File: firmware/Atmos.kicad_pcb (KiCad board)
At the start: 4 copper layers, 74 x 56 mm, 73 parts, among them J1 AS3935 breakout, J2 BME280 breakout, J3 USB_C_Receptacle_USB2.0_16P, J4 Micro_SD_Card, J5 Solar power input, J6 Amphenol 132134, Q1 PMOS_Substrate, Q2 PMOS_Substrate, Q3 PMOS_Substrate, SW2 SW_Push, U1 ESP32-S3-WROOM-1, U10 TPS22918DBVR, U11 MAX17048G_T10, U12 CN3791, U13 SGP40-D-R4, U2 AP2112K-3.3, U3 DS3231M, U4 PMS5003, U5 LTC4412xS6, U7 RFM95W-915S2, U8 USBLC6-2SC6, U9 TPS61023DRLR

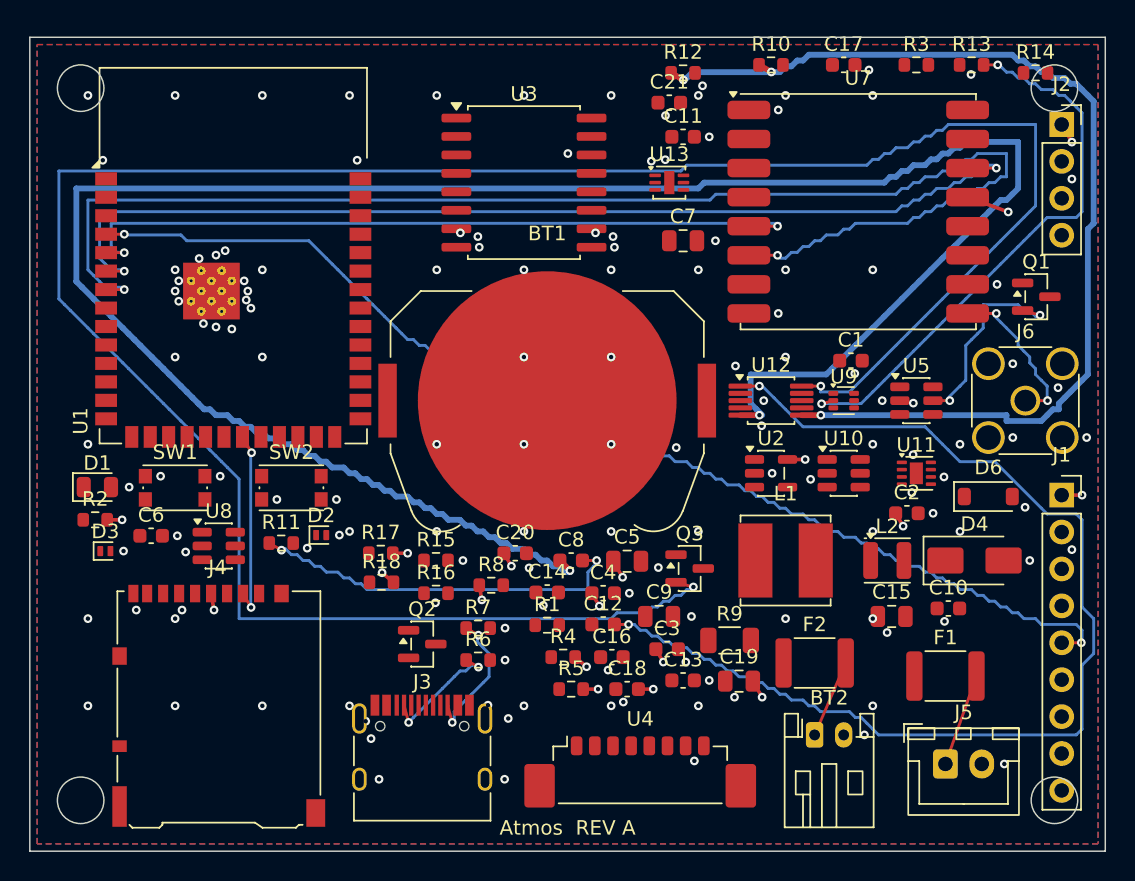
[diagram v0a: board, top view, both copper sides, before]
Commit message: PCB V1: finish routing with Freerouting (~99.85%, solid GND plane)
Completed the remaining ~45% of the board with Freerouting 2.2.4 (headless
CLI, local JRE). From 55% -> ~99.85% routed (1 of ~660 connections open),
0 shorts / 0 clearance / 0 hole-to-hole violations.

- Stackup: F.Cu signal / In1 solid GND plane / In2 +3V3+power+signal / B.Cu
  signal. Freeing In2 as a routing layer (vs locking both inner planes) was
  the key to a completable route.
- F.Cu GND pour stitched to the In1 plane with all-layer/hole/edge-aware vias.
- min_via_diameter 0.5 -> 0.4 mm (Freerouting emits 0.48 mm vias).
- 1 open connection: U13 (SGP40) GND, blocked by the placeholder DFN
  footprint; resolves when the real 2.44 mm land is placed.
- Respin note: move R14 (edge placement) next to U9.

Adds the reproducible Freerouting pipeline under tools/ and a full write-up
in docs/PCB-V1-NOTES.md.

Co-Authored-By: Claude Opus 4.8 <noreply@anthropic.com>
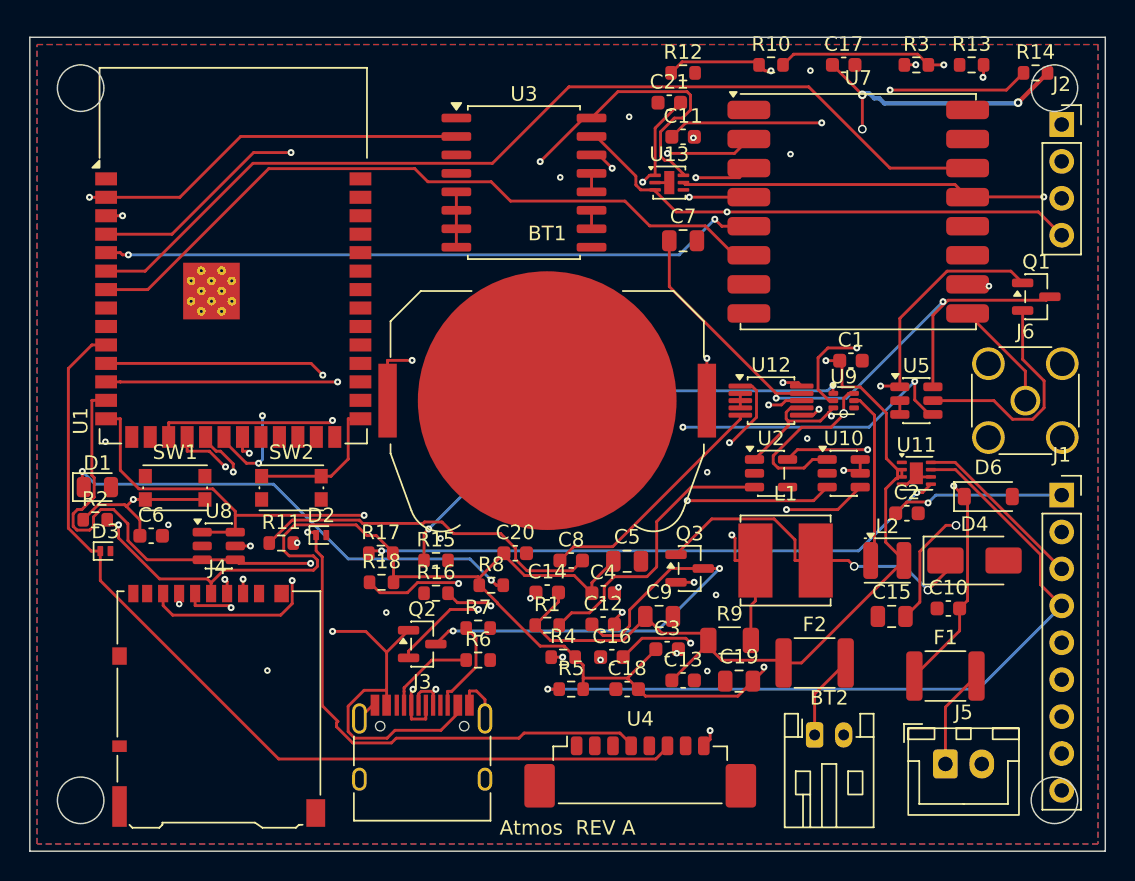
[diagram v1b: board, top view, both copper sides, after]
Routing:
- net +3V3: track 22.0 -> 224.8 mm, vias 18 -> 6
- net SCL: track 0.00 -> 163.4 mm, vias 0 -> 3
- net SDA: track 0.00 -> 151.3 mm, vias 0 -> 3
- net M1 gate: track 165.1 -> 18.9 mm
- net COM: track 147.1 -> 16.7 mm, vias 2 -> 0
- net VIN_CHG: track 0.00 -> 122.3 mm, vias 0 -> 5
- net +VBATT: track 0.00 -> 96.6 mm, vias 0 -> 3
- net +5V: track 0.00 -> 71.2 mm, vias 0 -> 5
- net SD_MISO: track 0.00 -> 69.1 mm, vias 0 -> 4
- net Net-(Q2-G): track 0.00 -> 68.6 mm, vias 0 -> 4
- net FB_BOOST: track 0.00 -> 66.4 mm, vias 0 -> 3
- net PMS_SET: track 0.00 -> 63.7 mm
- net SD_SCK: track 0.00 -> 62.5 mm, vias 0 -> 3
- net PMS_RX: track 0.00 -> 62.4 mm, vias 0 -> 2
- net SD_MOSI: track 0.00 -> 60.4 mm, vias 0 -> 3
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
